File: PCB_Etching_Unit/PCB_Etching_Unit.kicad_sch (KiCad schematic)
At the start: 89 parts, among them M1 Motor_DC, M2 Motor_DC, Q1 TIP42, Q10 TIP42, Q11 TIP41, Q12 2N3904, Q13 TIP42, Q14 BC550, Q15 BC550, Q16 BC550, Q17 BC550, Q18 BC550, Q19 BC550, Q2 TIP42, Q20 BC550, Q3 TIP42, Q4 TIP42, Q5 TIP42, Q6 TIP41, Q7 TIP41, Q8 TIP42, Q9 TIP41, SW1 SW_MEC_5G, SW2 SW_MEC_5G, SW3 SW_MEC_5G, SW4 SW_MEC_5G, SW5 SW_MEC_5G, SW6 SW_MEC_5G, SW7 SW_MEC_5G, U1 HDSP-7801, U11 4511, U2 HDSP-7801, U3 HDSP-7801, U4 HDSP-7801, U5 4027, U6 4027, U9 4011

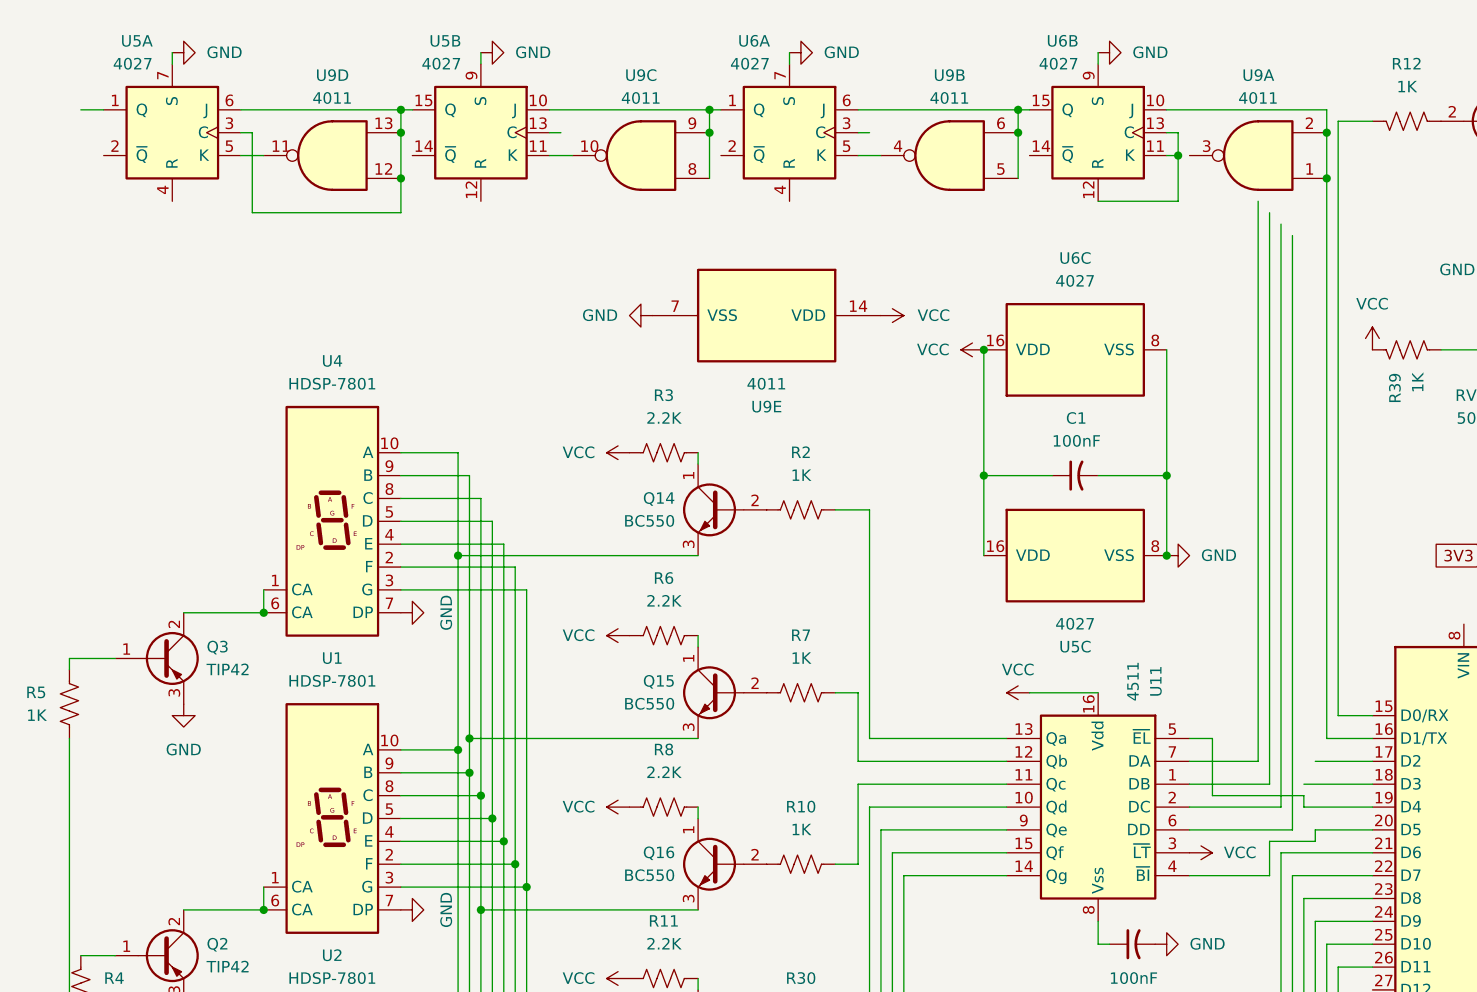
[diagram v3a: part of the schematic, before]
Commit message: Previously messed up shift register wiring. Fixed now
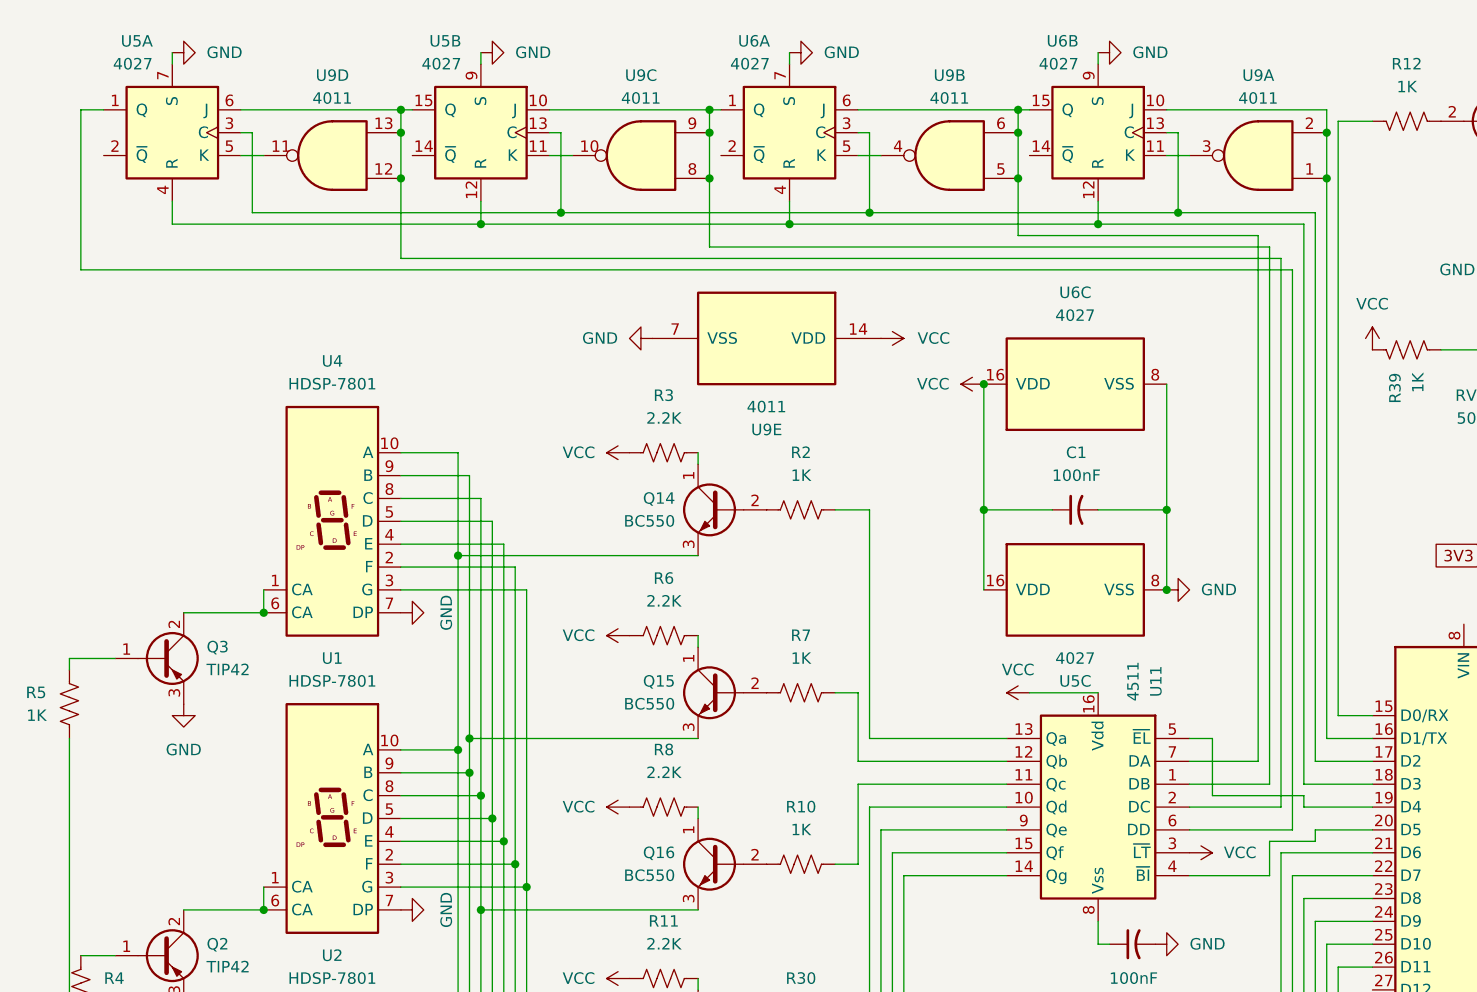
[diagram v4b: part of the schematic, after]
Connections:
- net at U5.15 (Q), U5.6 (J), U9.12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: now also U11.2 (DC); no longer U5.3 (C)
- net at U5.10 (J), U6.1 (Q), U9.8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: now also U11.1 (DB)
- net at U9.3: now also U6.11 (K)
- net at U5.12 (R): now also A1.18 (D3), U5.4 (R), U6.12 (R), U6.4 (R)
- net at U5.13 (C): now also A1.17 (D2), U5.3 (C), U6.13 (C), U6.3 (C)
- net at U6.15 (Q), U6.6 (J), U9.5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: now also U11.7 (DA)
- net at U11.6 (DD): now also U5.1 (Q)
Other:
- moved on the sheet: C1, U5C, U6C, U9E
